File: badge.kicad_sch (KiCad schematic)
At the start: 33 parts, among them J1 SAO V.1.69bis master, Q1 BSS138, SW1 power, SW2 SW_Push, SW3 update epaper, U1 Seeed XIAO ESP32-C3, U2 MH-ET_epaper_ 2.13, U3 5V boost converter, U4 TXS0104EPWR

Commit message: realign some tracks, add more vias stitching GND fills
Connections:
- net GND: no longer SW1.6 (C)
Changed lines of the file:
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@@
-    (stroke (width 0) (type default) (color 0 0 0 0))
-  )
-  (wire (pts (xy 30.48 100.33) (xy 30.48 102.87))
     (stroke (width 0) (type default) (color 0 0 0 0))
   )
@@
     (stroke (width 0) (type default) (color 0 0 0 0))
   )
-  (wire (pts (xy 30.48 83.82) (xy 33.02 83.82))
-    (stroke (width 0) (type default) (color 0 0 0 0))
-  )
   (wire (pts (xy 105.41 86.36) (xy 104.14 86.36))
     (stroke (width 0) (type default) (color 0 0 0 0))
@@
   )
   (wire (pts (xy 151.13 97.79) (xy 163.83 97.79))
-    (stroke (width 0) (type default) (color 0 0 0 0))
-  )
-  (wire (pts (xy 30.48 100.33) (xy 33.02 100.33))
     (stroke (width 0) (type default) (color 0 0 0 0))
   )
@@
     )
     (property "Datasheet" "" (id 3) (at 147.32 77.47 0)
-      (effects (font (size 1.27 1.27)) hide)
-    )
-    (pin "1")
-  )
-  (symbol (lib_id "power:GND") (at 30.48 102.87 0) (unit 1)
-    (in_bom yes) (on_board yes)
-    (property "Reference" "#PWR0107" (id 0) (at 30.48 109.22 0)
-      (effects (font (size 1.27 1.27)) hide)
-    )
-    (property "Value" "GND" (id 1) (at 30.48 107.95 0))
-    (property "Footprint" "" (id 2) (at 30.48 102.87 0)
-      (effects (font (size 1.27 1.27)) hide)
-    )
-    (property "Datasheet" "" (id 3) (at 30.48 102.87 0)
       (effects (font (size 1.27 1.27)) hide)
     )
@@
       (reference "#PWR0106") (unit 1) (value "GND") (footprint "")
     )
-    (path "/2b85703d-ddeb-4db4-9364-e6ffc24aa336"
-      (reference "#PWR0107") (unit 1) (value "GND") (footprint "")
-    )
     (path "/430835ad-a662-4737-a1dd-a4f9cab46650"

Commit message: add test points
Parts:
- added TP1: 0V, TestPoint:TestPoint_Pad_1.5x1.5mm, symbol Connector:TestPoint_Probe
- added TP10: D3clk, TestPoint:TestPoint_Pad_1.5x1.5mm, symbol Connector:TestPoint_Probe
- added TP11: D4in, TestPoint:TestPoint_Pad_1.5x1.5mm, symbol Connector:TestPoint_Probe
- added TP12: D4clk, TestPoint:TestPoint_Pad_1.5x1.5mm, symbol Connector:TestPoint_Probe
- added TP13: D5in, TestPoint:TestPoint_Pad_1.5x1.5mm, symbol Connector:TestPoint_Probe
- added TP14: D5clk, TestPoint:TestPoint_Pad_1.5x1.5mm, symbol Connector:TestPoint_Probe
- added TP15: Qin, TestPoint:TestPoint_Pad_1.5x1.5mm, symbol Connector:TestPoint_Probe
- added TP16: Qout, TestPoint:TestPoint_Pad_1.5x1.5mm, symbol Connector:TestPoint_Probe
- added TP17: LEDin, TestPoint:TestPoint_Pad_1.5x1.5mm, symbol Connector:TestPoint_Probe
- added TP18: /RST, TestPoint:TestPoint_Pad_1.5x1.5mm, symbol Connector:TestPoint_Probe
- added TP19: /CS, TestPoint:TestPoint_Pad_1.5x1.5mm, symbol Connector:TestPoint_Probe
- added TP2: 3.8V, TestPoint:TestPoint_Pad_1.5x1.5mm, symbol Connector:TestPoint_Probe
- added TP20: BUSY, TestPoint:TestPoint_Pad_1.5x1.5mm, symbol Connector:TestPoint_Probe
- added TP3: 3.3V, TestPoint:TestPoint_Pad_1.5x1.5mm, symbol Connector:TestPoint_Probe
- added TP4: 5V, TestPoint:TestPoint_Pad_1.5x1.5mm, symbol Connector:TestPoint_Probe
- added TP5: D1in, TestPoint:TestPoint_Pad_1.5x1.5mm, symbol Connector:TestPoint_Probe
- added TP6: D1clk, TestPoint:TestPoint_Pad_1.5x1.5mm, symbol Connector:TestPoint_Probe
- added TP7: D2in, TestPoint:TestPoint_Pad_1.5x1.5mm, symbol Connector:TestPoint_Probe
- added TP8: D2clk, TestPoint:TestPoint_Pad_1.5x1.5mm, symbol Connector:TestPoint_Probe
- added TP9: D3in, TestPoint:TestPoint_Pad_1.5x1.5mm, symbol Connector:TestPoint_Probe
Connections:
- net +3V3: now also TP3.1
- net +5V: now also TP4.1
- net BAT+: now also TP2.1
- net CS/OE: now also TP19.1
- net GND: now also TP1.1
- net GPIO2/BUSY: now also TP20.1
- net RESET/LED: now also TP15.1, TP18.1
- net ls_MOSI: now also TP5.1
- net ls_SCLK: now also TP6.1
- net at D6.1 (K), R11.1: now also TP17.1
- net at D2.6 (DO), D3.1 (DI): now also TP9.1
- net at D2.5 (CO), D3.2 (CI): now also TP10.1
- net at D3.5 (CO), D4.2 (CI): now also TP12.1
- net at D3.6 (DO), D4.1 (DI): now also TP11.1
- net at Q1.3 (D), R11.2: now also TP16.1
- net at D1.5 (CO), D2.2 (CI): now also TP8.1
- net at D1.6 (DO), D2.1 (DI): now also TP7.1
- net at D4.5 (CO), D5.2 (CI): now also TP14.1
- net at D4.6 (DO), D5.1 (DI): now also TP13.1

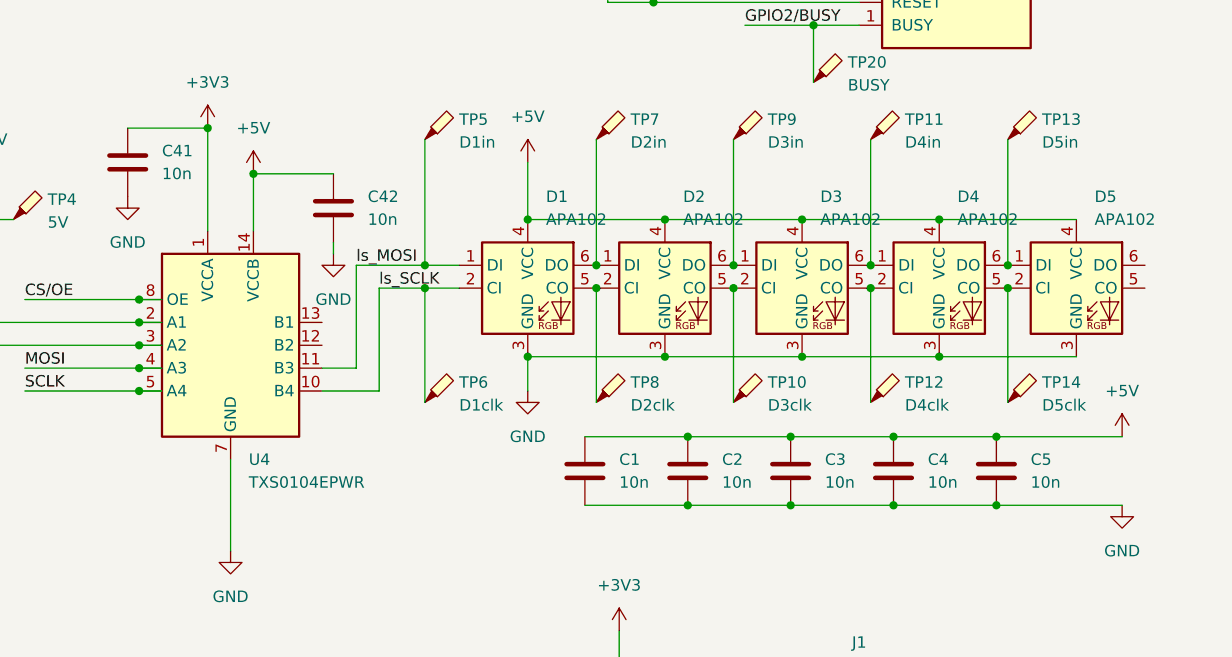
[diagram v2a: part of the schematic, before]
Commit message: bump up decoupling caps to non-trivial value; change font to Lobster Two
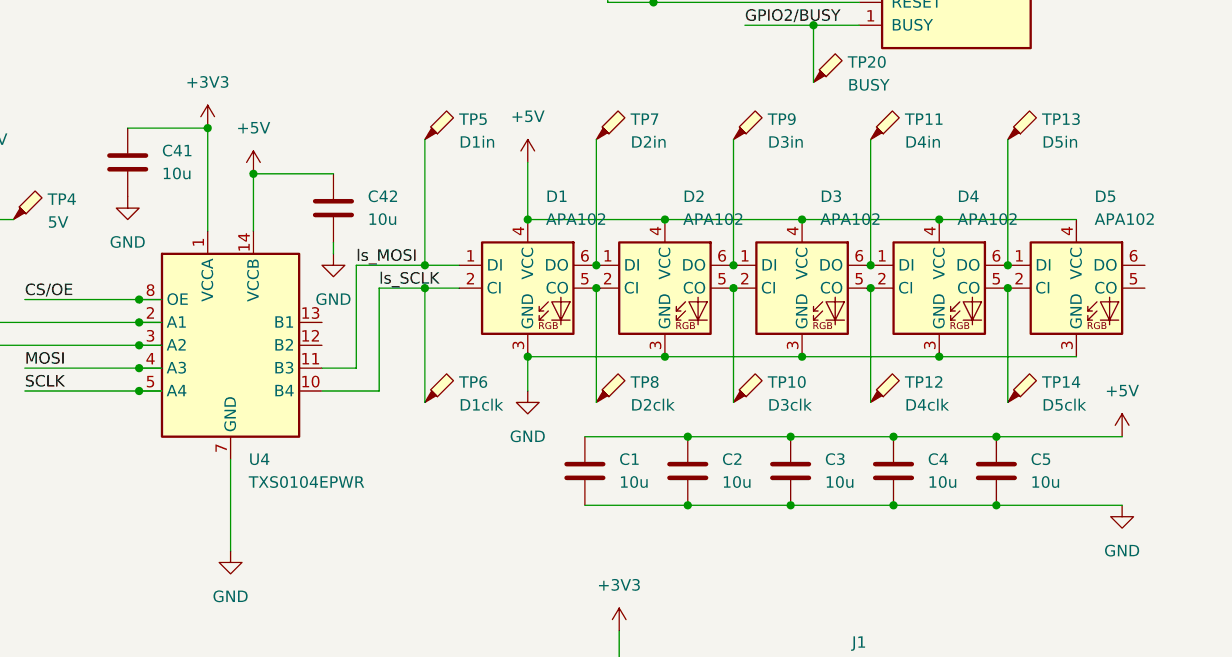
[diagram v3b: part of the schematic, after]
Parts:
- C1, C2, C3, C4, C41, C42, C5: value 10n -> 10u
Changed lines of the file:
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@@
       (effects (font (size 1.27 1.27)) (justify left))
     )
-    (property "Value" "10n" (at 166.37 76.1999 0)
+    (property "Value" "10u" (at 166.37 76.1999 0)
       (effects (font (size 1.27 1.27)) (justify left))
     )
@@
   (symbol (lib_id "Device:C") (at 224.79 109.22 0) (unit 1)
     (in_bom yes) (on_board yes) (dnp no) (fields_autoplaced)
-    (property "Reference" "C2" (at 228.6 107.9499 0)
-      (effects (font (size 1.27 1.27)) (justify left))
-    )
-    (property "Value" "10n" (at 228.6 110.4899 0)
+    (property "Reference" "C2" (at 228.6 107.95 0)
+      (effects (font (size 1.27 1.27)) (justify left))
+    )
+    (property "Value" "10u" (at 228.6 110.49 0)
       (effects (font (size 1.27 1.27)) (justify left))
     )
@@
   (symbol (lib_id "Device:C") (at 247.65 109.22 0) (unit 1)
     (in_bom yes) (on_board yes) (dnp no) (fields_autoplaced)
-    (property "Reference" "C4" (at 251.46 107.9499 0)
-      (effects (font (size 1.27 1.27)) (justify left))
-    )
-    (property "Value" "10n" (at 251.46 110.4899 0)
+    (property "Reference" "C4" (at 251.46 107.95 0)
+      (effects (font (size 1.27 1.27)) (justify left))
+    )
+    (property "Value" "10u" (at 251.46 110.49 0)
       (effects (font (size 1.27 1.27)) (justify left))
     )
@@
       (effects (font (size 1.27 1.27)) (justify left))
     )
-    (property "Value" "10n" (at 189.23 81.2799 0)
+    (property "Value" "10u" (at 189.23 81.2799 0)
       (effects (font (size 1.27 1.27)) (justify left))
     )
@@
   (symbol (lib_id "Device:C") (at 259.08 109.22 0) (unit 1)
     (in_bom yes) (on_board yes) (dnp no) (fields_autoplaced)
-    (property "Reference" "C5" (at 262.89 107.9499 0)
-      (effects (font (size 1.27 1.27)) (justify left))
-    )
-    (property "Value" "10n" (at 262.89 110.4899 0)
+    (property "Reference" "C5" (at 262.89 107.95 0)
+      (effects (font (size 1.27 1.27)) (justify left))
+    )
+    (property "Value" "10u" (at 262.89 110.49 0)
       (effects (font (size 1.27 1.27)) (justify left))
     )
@@
       (effects (font (size 1.27 1.27)) (justify left))
     )
-    (property "Value" "10n" (at 217.17 110.4899 0)
+    (property "Value" "10u" (at 217.17 110.4899 0)
       (effects (font (size 1.27 1.27)) (justify left))
     )
@@
   (symbol (lib_id "Device:C") (at 236.22 109.22 0) (unit 1)
     (in_bom yes) (on_board yes) (dnp no) (fields_autoplaced)
-    (property "Reference" "C3" (at 240.03 107.9499 0)
-      (effects (font (size 1.27 1.27)) (justify left))
-    )
-    (property "Value" "10n" (at 240.03 110.4899 0)
-      (effects (font (size 1.27 1.27)) (justify left))
-    )
+    (property "Reference" "C3" (at 240.03 107.95 0)
+      (effects (font (size 1.27 1.27)) (justify left))
+    )
+    (property "Value" "10u" (at 240.03 110.49 0)
+      (effects (font (size 1.27 1.27)) (justify left))
+    )

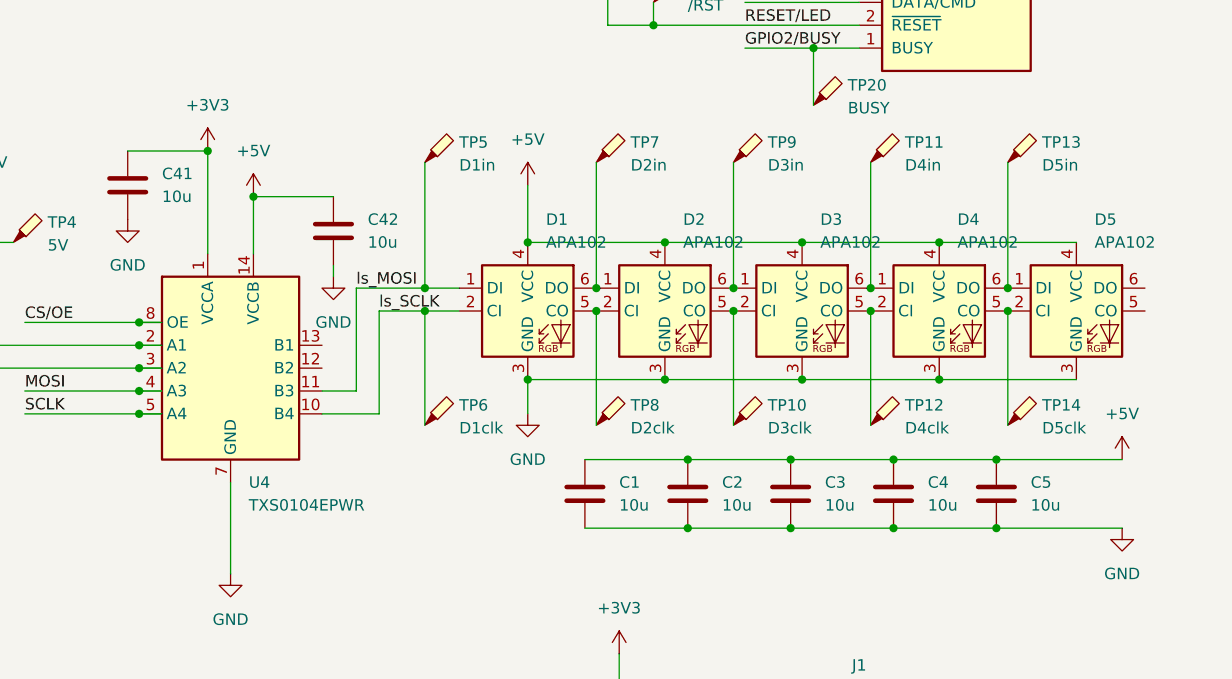
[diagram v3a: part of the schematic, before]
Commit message: updated decoupling cap value; tweaked testpoint locations & silkscreen
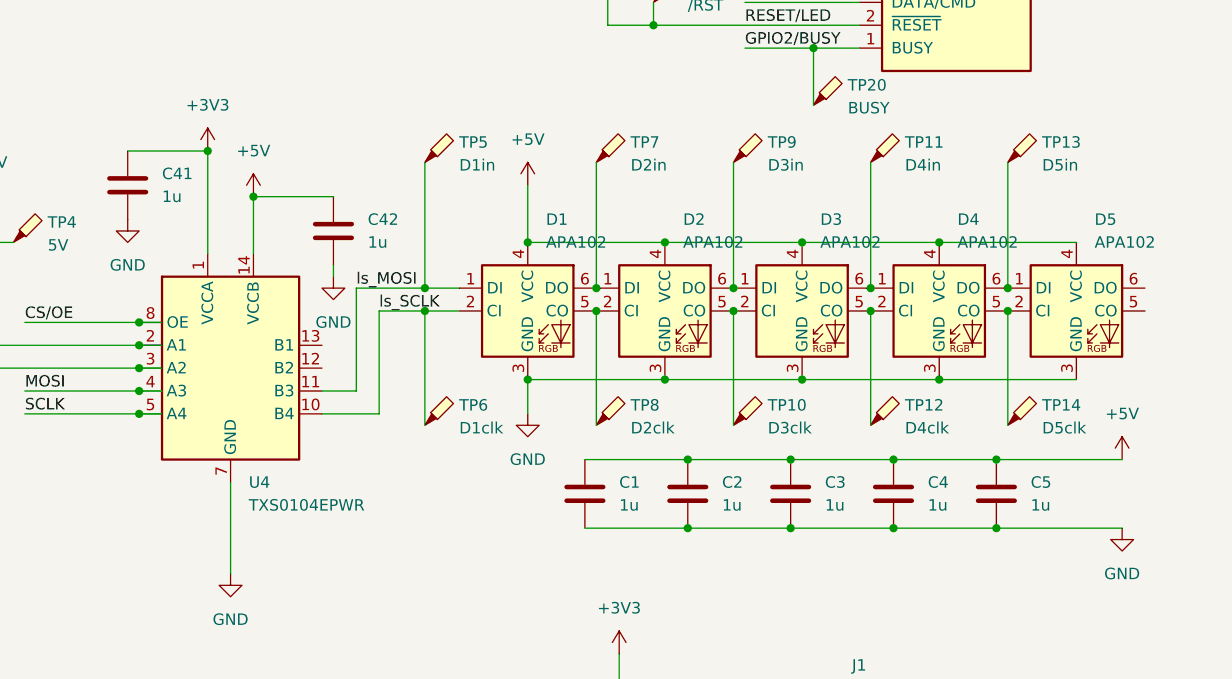
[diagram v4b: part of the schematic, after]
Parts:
- C1, C2, C3, C4, C41, C42, C5: value 10u -> 1u
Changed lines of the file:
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@@
   (symbol (lib_id "Device:C") (at 162.56 74.93 0) (unit 1)
     (in_bom yes) (on_board yes) (dnp no) (fields_autoplaced)
-    (property "Reference" "C41" (at 166.37 73.6599 0)
-      (effects (font (size 1.27 1.27)) (justify left))
-    )
-    (property "Value" "10u" (at 166.37 76.1999 0)
+    (property "Reference" "C41" (at 166.37 73.66 0)
+      (effects (font (size 1.27 1.27)) (justify left))
+    )
+    (property "Value" "1u" (at 166.37 76.2 0)
       (effects (font (size 1.27 1.27)) (justify left))
     )
@@
       (effects (font (size 1.27 1.27)) (justify left))
     )
-    (property "Value" "10u" (at 228.6 110.49 0)
+    (property "Value" "1u" (at 228.6 110.49 0)
       (effects (font (size 1.27 1.27)) (justify left))
     )
@@
       (effects (font (size 1.27 1.27)) (justify left))
     )
-    (property "Value" "10u" (at 251.46 110.49 0)
+    (property "Value" "1u" (at 251.46 110.49 0)
       (effects (font (size 1.27 1.27)) (justify left))
     )
@@
   (symbol (lib_id "Device:C") (at 185.42 80.01 0) (unit 1)
     (in_bom yes) (on_board yes) (dnp no) (fields_autoplaced)
-    (property "Reference" "C42" (at 189.23 78.7399 0)
-      (effects (font (size 1.27 1.27)) (justify left))
-    )
-    (property "Value" "10u" (at 189.23 81.2799 0)
+    (property "Reference" "C42" (at 189.23 78.74 0)
+      (effects (font (size 1.27 1.27)) (justify left))
+    )
+    (property "Value" "1u" (at 189.23 81.28 0)
       (effects (font (size 1.27 1.27)) (justify left))
     )
@@
       (effects (font (size 1.27 1.27)) (justify left))
     )
-    (property "Value" "10u" (at 262.89 110.49 0)
+    (property "Value" "1u" (at 262.89 110.49 0)
       (effects (font (size 1.27 1.27)) (justify left))
     )
@@
   (symbol (lib_id "Device:C") (at 213.36 109.22 0) (unit 1)
     (in_bom yes) (on_board yes) (dnp no) (fields_autoplaced)
-    (property "Reference" "C1" (at 217.17 107.9499 0)
-      (effects (font (size 1.27 1.27)) (justify left))
-    )
-    (property "Value" "10u" (at 217.17 110.4899 0)
+    (property "Reference" "C1" (at 217.17 107.95 0)
+      (effects (font (size 1.27 1.27)) (justify left))
+    )
+    (property "Value" "1u" (at 217.17 110.49 0)
       (effects (font (size 1.27 1.27)) (justify left))
     )
@@
       (effects (font (size 1.27 1.27)) (justify left))
     )
-    (property "Value" "10u" (at 240.03 110.49 0)
-      (effects (font (size 1.27 1.27)) (justify left))
-    )
+    (property "Value" "1u" (at 240.03 110.49 0)
+      (effects (font (size 1.27 1.27)) (justify left))
+    )
